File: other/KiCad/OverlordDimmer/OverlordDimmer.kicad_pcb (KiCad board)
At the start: 2 copper layers, 155.7 x 86.3 mm, 252 parts, among them J1 1757310, J2 1757310, J3 Conn_01x12_Pin, J4 Conn_01x04_Pin, J5 Conn_01x04_Pin, Q1 2N3904, Q10 IRF740, Q11 2N3906, Q12 IRF740, Q13 2N3904, Q14 IRF740, Q15 2N3906, Q16 IRF740, Q17 2N3904, Q18 IRF740, Q19 2N3906, Q2 IRF740, Q20 IRF740, Q21 2N3904, Q22 IRF740, Q23 2N3906, Q24 IRF740, Q25 2N3904, Q26 IRF740, Q27 2N3906, Q28 IRF740, Q29 2N3904, Q3 2N3906, Q30 IRF740, Q31 2N3906, Q32 IRF740, Q33 2N3904, Q34 IRF740, Q35 2N3906, Q36 IRF740, Q37 2N3904, Q38 IRF740, Q39 2N3906, Q4 IRF740, Q40 IRF740, Q41 BC817, Q42 2SC4061KT146N, Q43 2SC4061KT146N, Q5 2N3904, Q6 IRF740, Q7 2N3906, Q8 IRF740, Q9 2N3904, U1 4N25, U10 4N25, U11 SN65HVD230, U2 4N25, U3 4N25, U4 4N25, U5 4N25, U6 4N25, U7 4N25, U8 4N25, U9 4N25

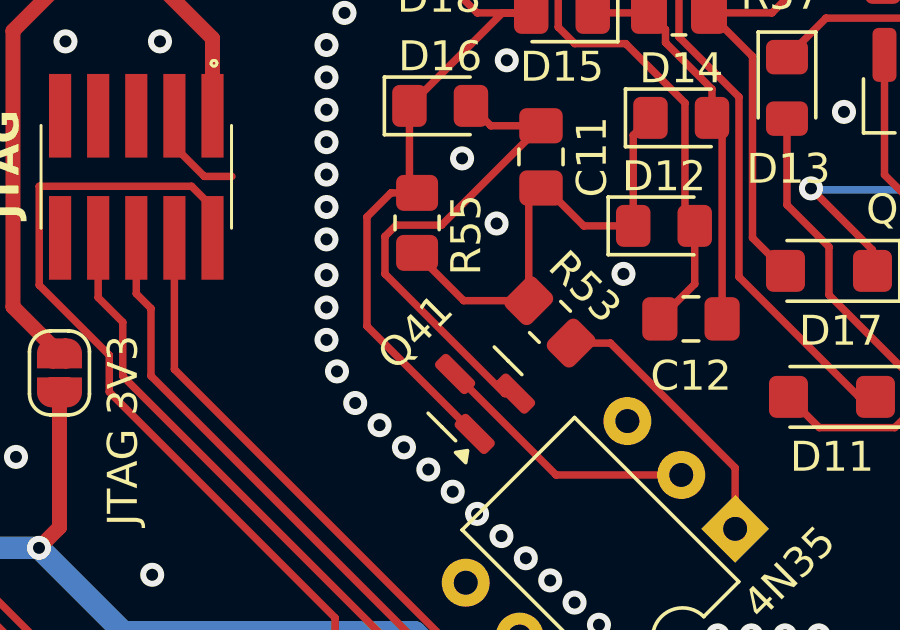
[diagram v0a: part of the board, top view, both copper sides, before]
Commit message: update to latest rtdb_gen
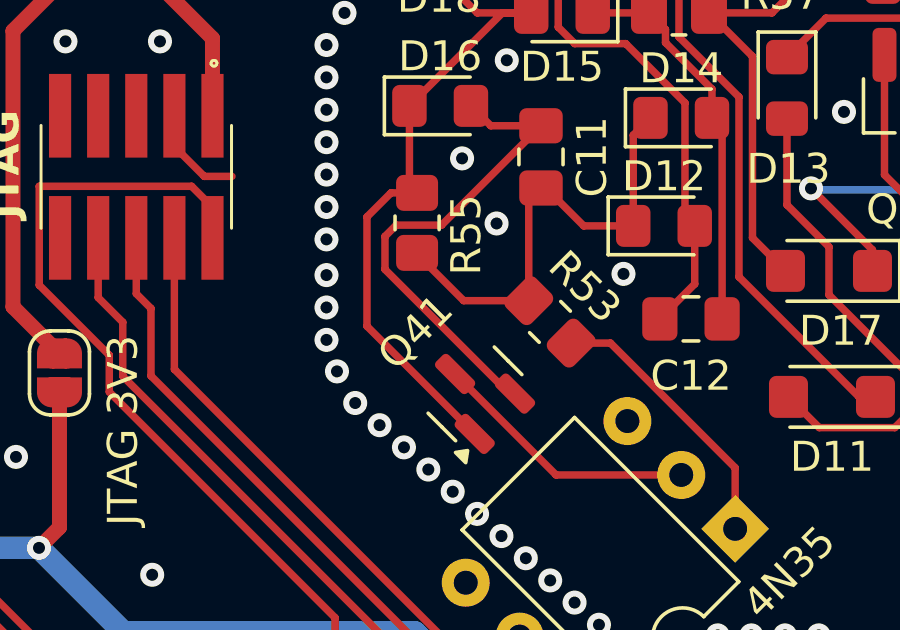
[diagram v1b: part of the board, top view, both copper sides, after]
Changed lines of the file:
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@@
 		(fp_arc
 			(start -5.6 9.6)
-			(mid -5.500001 9.500009)
+			(mid -5.500001 9.50001)
 			(end -5.400001 9.6)
 			(stroke
@@
 		(fp_arc
 			(start -5.6 9.6)
-			(mid -5.500001 9.500009)
+			(mid -5.500001 9.50001)
 			(end -5.400001 9.6)
 			(stroke
@@
 	)
 	(segment
-		(start 54.1 39.4)
-		(end 58.091161 43.391161)
+		(start 54.1 38.1499)
+		(end 54.1 39.2501)
 		(width 0.25)
 		(layer "F.Cu")
@@
 	)
 	(segment
-		(start 58.091161 43.391161)
-		(end 58.434664 43.391161)
+		(start 54.4749 37.775)
+		(end 54.1 38.1499)
 		(width 0.25)
 		(layer "F.Cu")
@@
 	)
 	(segment
-		(start 57.627499 34.4625)
-		(end 56.964999 33.8)
+		(start 59.3 34.4625)
+		(end 55.9875 37.775)
 		(width 0.25)
 		(layer "F.Cu")
@@
 	)
 	(segment
-		(start 54.1 38.1499)
-		(end 54.1 39.4)
+		(start 54.1 39.2501)
+		(end 58.241061 43.391161)
 		(width 0.25)
 		(layer "F.Cu")
@@
 	)
 	(segment
-		(start 59.3 34.4625)
-		(end 57.627499 34.4625)
+		(start 57.627499 34.4625)
+		(end 56.964999 33.8)
 		(width 0.25)
 		(layer "F.Cu")
@@
 	(segment
 		(start 59.3 34.4625)
-		(end 55.9875 37.775)
+		(end 57.627499 34.4625)
 		(width 0.25)
 		(layer "F.Cu")
@@
 	)
 	(segment
-		(start 54.4749 37.775)
-		(end 54.1 38.1499)
+		(start 58.241061 43.391161)
+		(end 58.434664 43.391161)
 		(width 0.25)
 		(layer "F.Cu")

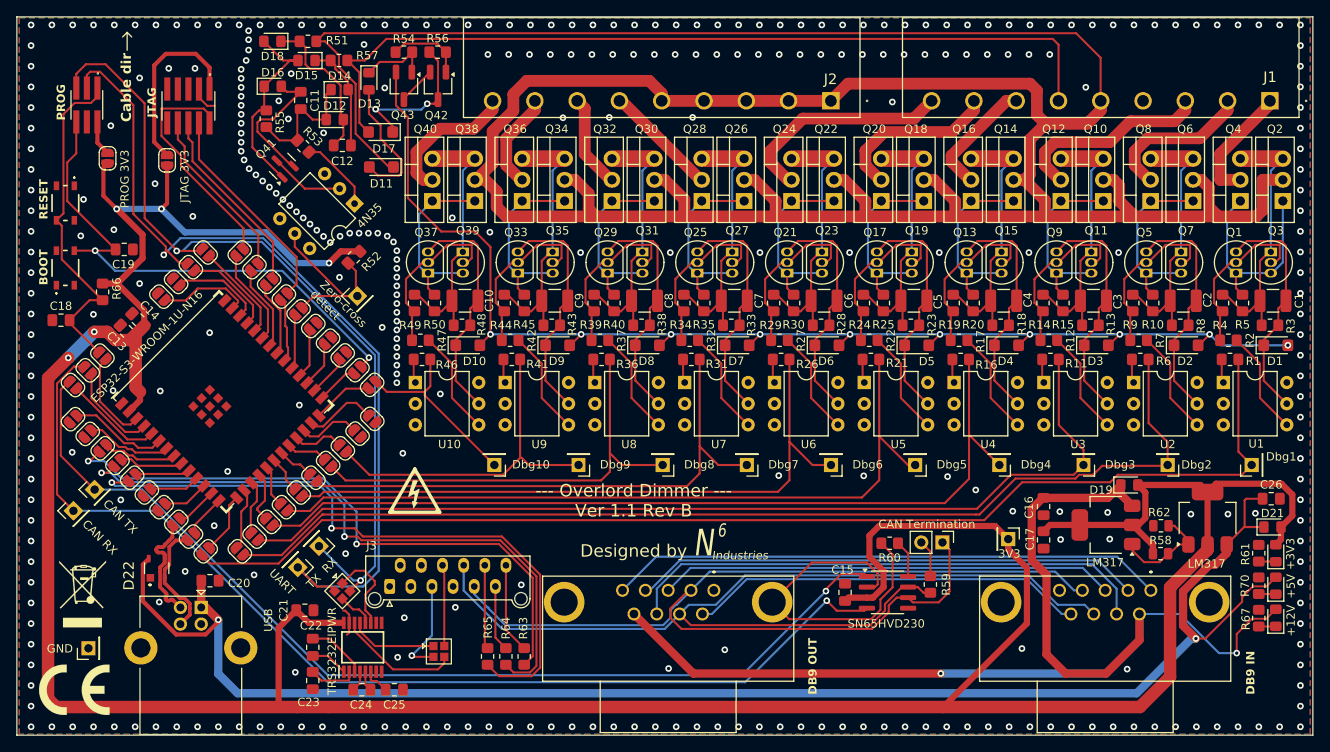
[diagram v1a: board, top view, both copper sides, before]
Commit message: Sent for PCB production, ver 1.2 rev A
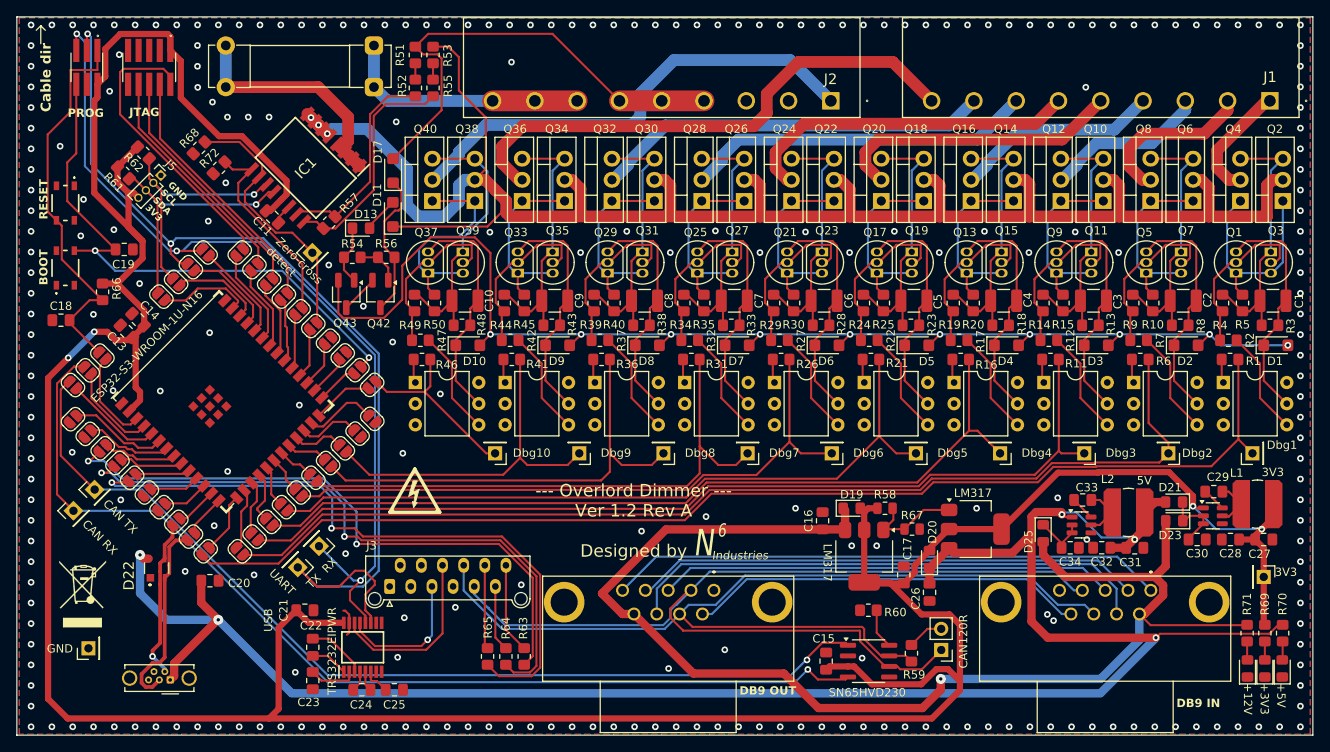
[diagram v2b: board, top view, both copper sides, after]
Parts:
- removed C12: 1nF, Capacitor_SMD:C_0805_2012Metric_Pad1.18x1.45mm_HandSolder
- removed D12, D14, D15, D16, D18: 1N4148, Diode_SMD:D_0805_2012Metric_Pad1.15x1.40mm_HandSolder
- removed JP41, JP49: SolderJumper_2_Open, Jumper:SolderJumper-2_P1.3mm_Open_RoundedPad1.0x1.5mm
- removed J_USB1: USB_B, Connector_USB:USB_B_Lumberg_2411_02_Horizontal
- removed Q41: BC817, Package_TO_SOT_SMD:SOT-23
- removed SYM4: CE, Symbol:CE-Logo_8.5x6mm_SilkScreen
- removed U_4N35_1: 4N35, Package_DIP:DIP-6_W7.62mm
- added C27: 22uF, Capacitor_SMD:C_0805_2012Metric_Pad1.18x1.45mm_HandSolder, F.Cu at (175.0, 88.2)
- added C28: 22uF, Capacitor_SMD:C_0805_2012Metric_Pad1.18x1.45mm_HandSolder, F.Cu at (171.0, 88.2)
- added C29: 0.1uF, Capacitor_SMD:C_0805_2012Metric_Pad1.18x1.45mm_HandSolder, F.Cu at (169.0, 82.5)
- added C30: 10uF, Capacitor_SMD:C_0805_2012Metric_Pad1.18x1.45mm_HandSolder, F.Cu at (167.0, 88.2)
- added C31: 22uF, Capacitor_SMD:C_0805_2012Metric_Pad1.18x1.45mm_HandSolder, F.Cu at (159.5, 89.2)
- added C32: 22uF, Capacitor_SMD:C_0805_2012Metric_Pad1.18x1.45mm_HandSolder, F.Cu at (155.5, 89.2)
- added C33: 0.1uF, Capacitor_SMD:C_0805_2012Metric_Pad1.18x1.45mm_HandSolder, F.Cu at (153.2, 83.5)
- added C34: 10uF, Capacitor_SMD:C_0805_2012Metric_Pad1.18x1.45mm_HandSolder, F.Cu at (151.8, 89.2)
- added D20: 1N4148, Diode_SMD:D_0805_2012Metric_Pad1.15x1.40mm_HandSolder, F.Cu at (134.8, 90.6)
- added D23: 1N4148, Diode_SMD:D_0805_2012Metric_Pad1.15x1.40mm_HandSolder, F.Cu at (164.2, 86.0)
- added D25: 1N4148, Diode_SMD:D_0805_2012Metric_Pad1.15x1.40mm_HandSolder, F.Cu at (148.5, 87.5)
- added F1: Fuse_Small, Fuse:Fuseholder_Clip-5x20mm_Bel_FC-203-22_Lateral_P17.80x5.00mm_D1.17mm_Horizontal, F.Cu at (68.1, 33.9)
- added IC1: ACS37800KMACTR-090B3-I2C, OverlordCommon:SOIC127P1030X265-16N, F.Cu at (59.9, 43.6)
- added L1: 3.9uH, Inductor_SMD:L_Bourns_SDR0604, F.Cu at (174.2, 84.0)
- added L2: 4.7uH, Inductor_SMD:L_Bourns_SDR0604, F.Cu at (158.8, 85.0)
- added R68: 4k7, Resistor_SMD:R_0805_2012Metric_Pad1.20x1.40mm_HandSolder, F.Cu at (47.1, 41.2)
- added R69: 60, Resistor_SMD:R_0805_2012Metric_Pad1.20x1.40mm_HandSolder, F.Cu at (175.1, 99.5)
- added R71: 499, Resistor_SMD:R_0805_2012Metric_Pad1.20x1.40mm_HandSolder, F.Cu at (173.0, 99.5)
- added R72: 4k7, Resistor_SMD:R_0805_2012Metric_Pad1.20x1.40mm_HandSolder, F.Cu at (49.5, 43.6)
- added U12: AP63203WU, Package_TO_SOT_SMD:TSOT-23-6, F.Cu at (168.9, 85.4)
- added U13: AP63205WU, Package_TO_SOT_SMD:TSOT-23-6, F.Cu at (153.1, 86.5)
- C11: value 10uF -> 0.1uF
- J4: value Conn_01x04_Pin -> USB_B_Micro; footprint OverlordCommon:Solder_select_2x2 -> Connector_USB:USB_Micro-B_Wuerth_614105150721_Vertical_CircularHoles
- J5: value Conn_01x04_Pin -> I2C; footprint OverlordCommon:Solder_select_2x2 -> Connector_PinHeader_1.27mm:PinHeader_1x04_P1.27mm_Vertical
- R51: value 220k -> 1M
- R52: value 2.2k -> 1M
- R53: value 1k -> 1M
- R55: value 22k -> 1M
- R57: value 220k -> 8k2
- R61: value 60 -> 10k
- R62: value 390 -> 10k; footprint Resistor_SMD:R_0805_2012Metric -> Resistor_SMD:R_0805_2012Metric_Pad1.20x1.40mm_HandSolder
- R67: value 499 -> 390; footprint Resistor_SMD:R_0805_2012Metric_Pad1.20x1.40mm_HandSolder -> Resistor_SMD:R_0805_2012Metric
- moved R61 143.9 mm to (38.0, 44.2), turned to 135 degrees
- moved R62 130.2 mm to (40.4, 41.8), turned to 135 degrees
- moved J5 54.5 mm to (42.5, 44.5)
- moved R67 43.0 mm to (132.8, 87.0), turned to 0 degrees
- moved C26 42.6 mm to (134.8, 94.6), turned to -90 degrees
- moved R58 33.5 mm to (129.5, 84.5)
- moved D19 33.5 mm to (125.5, 84.5)
- moved J4 32.5 mm to (43.6, 105.1), turned to 180 degrees
- moved Dbg3V3_1 31.0 mm to (175.0, 92.8)
- moved U_LM317_1 29.3 mm to (127.0, 90.2), turned to -90 degrees
- moved U_LM317_2 27.9 mm to (140.3, 87.0), turned to 0 degrees
- moved C16 26.6 mm to (122.0, 86.0), turned to 90 degrees
- moved Q42 25.9 mm to (68.9, 58.8)
- moved Q43 25.9 mm to (64.8, 58.8)
- moved R54 25.4 mm to (65.5, 54.4), turned to 0 degrees
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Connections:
- 12VLED1 pad 1: Net-(12VLED1-K) -> GND
- 12VLED1 pad 2: +12V -> Net-(12VLED1-A)
- 3V3LED1 pad 1: Net-(3V3LED1-K) -> GND
- 3V3LED1 pad 2: +3.3V -> Net-(3V3LED1-A)
- 5VLED1 pad 1: Net-(5VLED1-K) -> GND
- 5VLED1 pad 2: +5V -> Net-(5VLED1-A)
- C11 pad 1: Net-(D12-K) -> +3.3V
- C11 pad 2: Net-(D16-A) -> GND
- D11 pad 1: L -> L_OUT
- D21 pad 1: +5V -> Net-(D21-K)
- D21 pad 2: +3.3V -> +5V
- J1 pad 4: GND -> OUT4
- J1 pad 5: L -> OUT5
- J1 pad 6: N -> OUT6
- J1 pad 7: OUT4 -> OUT7
- J1 pad 8: OUT5 -> OUT8
- J1 pad 9: OUT6 -> OUT9
- J2 pad 1: L -> OUT10
- J2 pad 2: L -> GND
- J2 pad 3: L -> GND
- J2 pad 4: L -> N
- J2 pad 5: L -> N
- J2 pad 6: OUT7 -> N
- J2 pad 7: OUT8 -> L
- J2 pad 8: OUT9 -> L
- J2 pad 9: OUT10 -> L
- J4 pad 1: Net-(J4-Pin_1) -> +5V
- J4 pad 2: Net-(J4-Pin_2) -> D-
- J4 pad 3: RS232_RX -> D+
- J4 pad 4: RS232_TX -> unconnected-(J4-ID-Pad4)
- J5 pad 1: Net-(J5-Pin_1) -> GND
- J5 pad 2: Net-(J5-Pin_2) -> SCL
- J5 pad 3: UART_RX_0 -> SDA
- J5 pad 4: UART_TX_0 -> +3.3V
- JP1 pad 2: unconnected-(JP1-B-Pad2) -> SDA
- JP17 pad 2: EDGE_DETECT -> UNDERV_DETECT
- JP19 pad 2: unconnected-(JP19-B-Pad2) -> EDGE_DETECT
- JP3 pad 2: unconnected-(JP3-B-Pad2) -> SCL
- J_JTAG2 pad 1: Net-(JP41-A) -> +3.3V
- J_PROG1 pad 2: Net-(JP49-A) -> +3.3V
- Q10 pad 2: L -> L_OUT
- Q14 pad 2: L -> L_OUT
- Q18 pad 2: L -> L_OUT
- Q2 pad 2: L -> L_OUT
- Q22 pad 2: L -> L_OUT
- Q26 pad 2: L -> L_OUT
- Q30 pad 2: L -> L_OUT
- Q34 pad 2: L -> L_OUT
- Q38 pad 2: L -> L_OUT
- Q6 pad 2: L -> L_OUT
- R51 pad 1: L -> N
- R51 pad 2: Net-(D12-A) -> Net-(R51-Pad2)
- R52 pad 1: +3.3V -> Net-(R51-Pad2)
- R52 pad 2: EDGE_DETECT -> Net-(IC1-VINN)
- R53 pad 1: Net-(D12-K) -> L_OUT
- R55 pad 1: Net-(D15-A) -> Net-(R53-Pad2)
- R55 pad 2: Net-(D12-K) -> Net-(IC1-VINP)
- R57 pad 1: N -> Net-(IC1-VINN)
- R57 pad 2: Net-(D14-A) -> Net-(IC1-VINP)
- R61 pad 1: Net-(3V3LED1-K) -> SDA
- R61 pad 2: GND -> +3.3V
- R62 pad 1: V_ADJ -> SCL
- R62 pad 2: GND -> +3.3V
- R67 pad 1: Net-(12VLED1-K) -> V_ADJ
- R70 pad 1: Net-(5VLED1-K) -> +5V
- R70 pad 2: GND -> Net-(5VLED1-A)
- U_TRS3232EIPWR1 pad 11: Net-(J5-Pin_1) -> UART_TX_0
- U_TRS3232EIPWR1 pad 12: Net-(J5-Pin_2) -> UART_RX_0
- U_TRS3232EIPWR1 pad 13: Net-(J4-Pin_1) -> RS232_TX
- U_TRS3232EIPWR1 pad 14: Net-(J4-Pin_2) -> RS232_RX
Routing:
- net L: track 377.1 -> 30.1 mm
- net L_OUT: track 0.00 -> 219.4 mm, vias 0 -> 3
- net OUT9: track 11.8 -> 64.4 mm
- net N: track 103.2 -> 56.8 mm
- net GND: track 48.2 -> 5.93 mm, vias 337 -> 258
- net OUT10: track 17.1 -> 57.6 mm
- net OUT8: track 11.3 -> 47.6 mm
- net +5V: track 202.8 -> 236.7 mm, vias 2 -> 5
- net SDA: track 0.00 -> 32.2 mm, vias 0 -> 1
- net SCL: track 0.00 -> 30.2 mm, vias 0 -> 1
- net L_IN: track 0.00 -> 28.6 mm
- net OUT7: track 13.8 -> 42.0 mm
- net Net-(IC1-VINP): track 0.00 -> 27.6 mm
- net Net-(IC1-VINN): track 0.00 -> 25.4 mm
- net Net-(D15-A): track 24.1 -> 0.00 mm
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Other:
- board text added: "--- Overlord Dimmer --- Ver 1.2 Rev A Designed by"
- board text added: "5V"
- board text added: "CAN120R"
- board text added: "GND SCL SDA 3V3"
- board text removed: "--- Overlord Dimmer --- Ver 1.1 Rev B Designed by"
- board text removed: "4N35"
- board text removed: "CAN Termination"
- board text removed: "JTAG 3V3"
- board text removed: "PROG 3V3"
